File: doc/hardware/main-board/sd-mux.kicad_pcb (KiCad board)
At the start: 2 copper layers, 50 x 132 mm, 54 parts, among them J1 SDCARD, P1 USB_OTG, P10 MKDS 1,5/3, P2 629105136821, P3 61400416021, P4 61400416021, P5 IDC_02X04, P6 IDC_02X04, P7 MKDS 1,5/3, Q1 IRF7606PBF, Q2 IRF7606PBF, Q3 IRF7606PBF, Q4 IRF7606PBF, Q5 2N7002, Q6 2N7002, Q7 IRF7606PBF, Q8 IRF7606PBF, U1 TS3USB30EDGSR, U2 FT245RL, U3 74AHC1G14, U4 TS3A27518E, U5 74AHC1G14

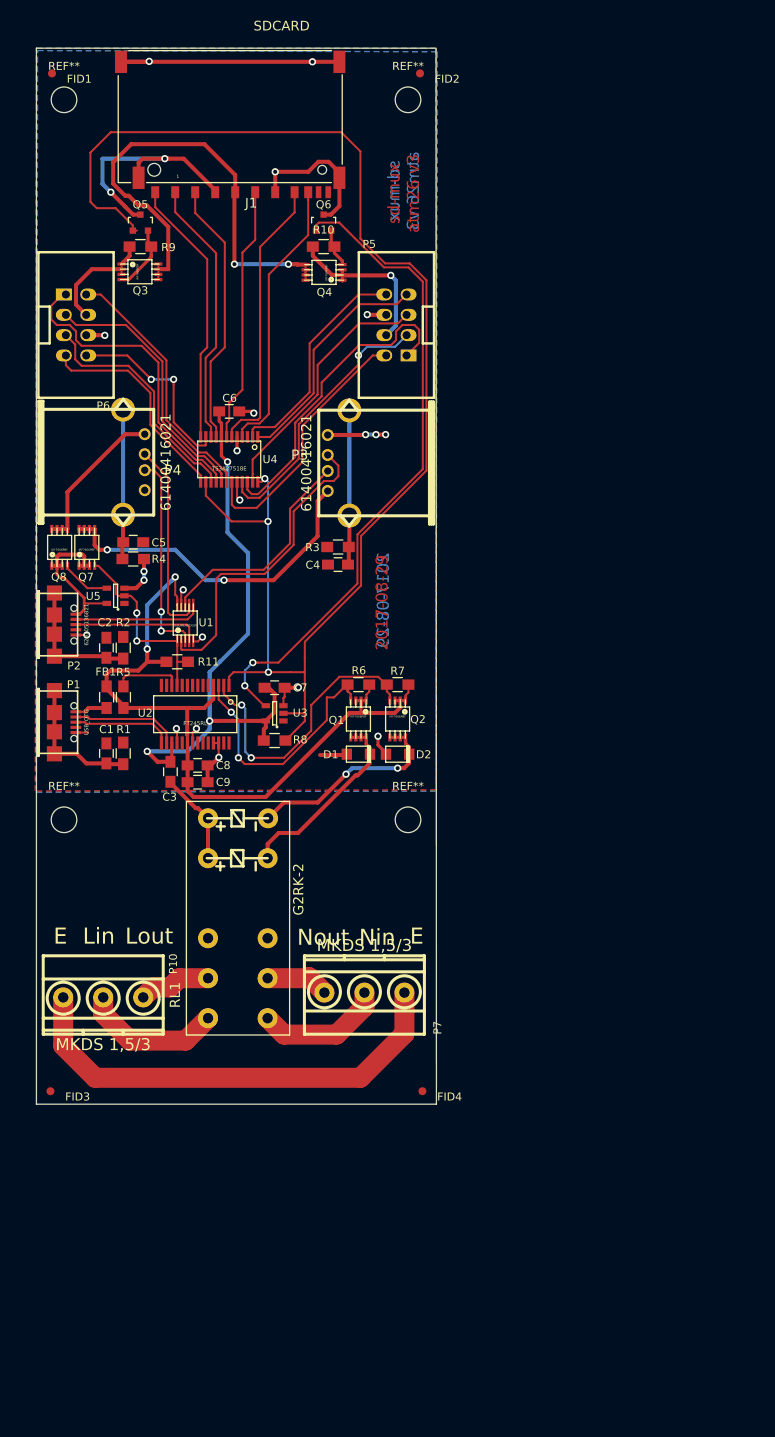
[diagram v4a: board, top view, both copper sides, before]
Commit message: Tweak pours to increase clearances.  Add some keepouts around ICs where lacking soldermask is likely to be problematic
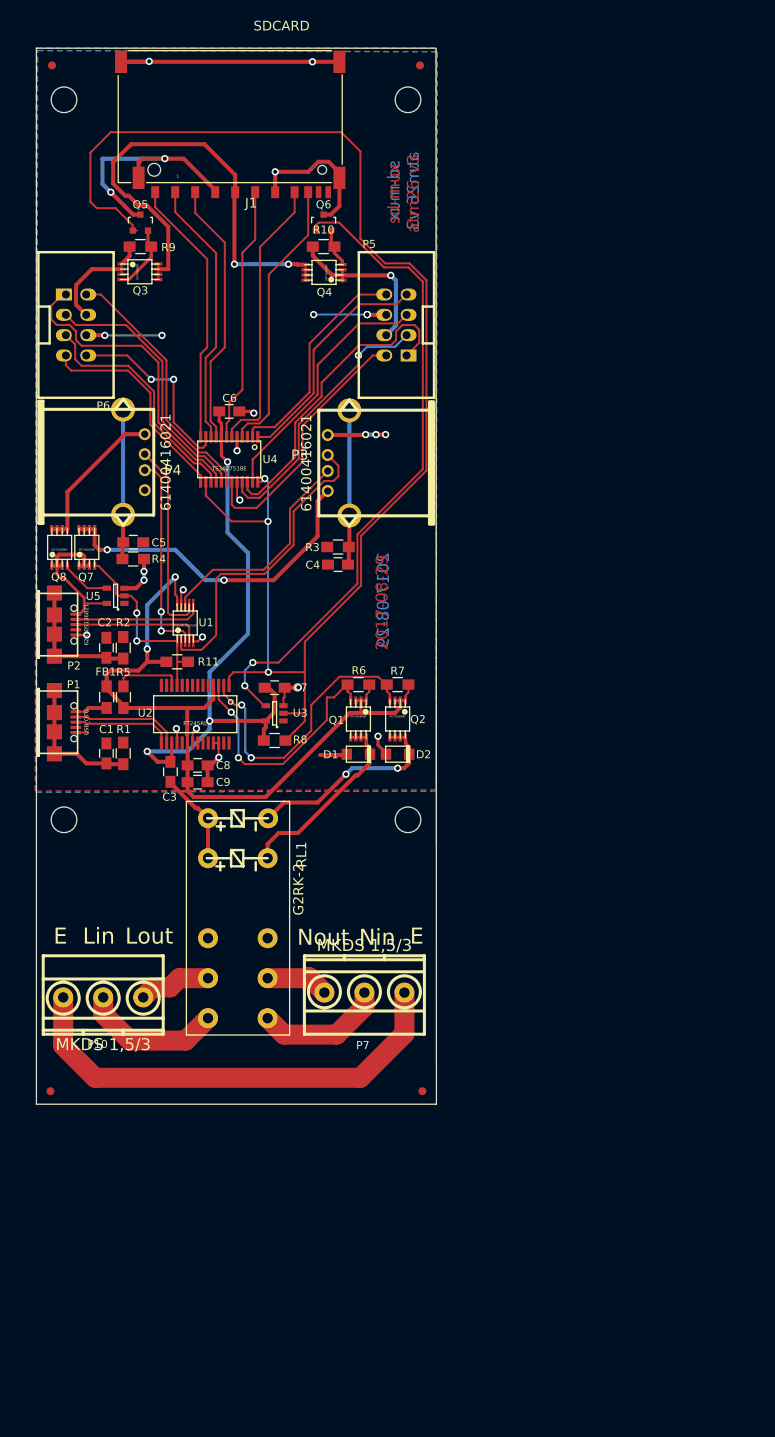
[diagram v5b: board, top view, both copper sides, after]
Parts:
- moved FID1 1.00 mm to (120.1, 17.8)
- moved FID2 1.00 mm to (166.1, 17.8)
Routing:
- net GND: track 143.3 -> 157.1 mm, vias 23 -> 26
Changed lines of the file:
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@@
     (thickness 1.6)
     (drawings 19)
-    (tracks 727)
+    (tracks 731)
     (zones 0)
     (modules 54)
@@
   )
   (setup
-    (last_trace_width 0.508)
+    (last_trace_width 0.254)
     (user_trace_width 0.508)
     (user_trace_width 1.116)
     (user_trace_width 2.5)
     (trace_clearance 0.2)
-    (zone_clearance 0.254)
+    (zone_clearance 0.508)
     (zone_45_only yes)
     (trace_min 0.254)
@@
     (pcbplotparams
       (layerselection 0x010fc_80000001)
-      (usegerberextensions false)
+      (usegerberextensions true)
       (excludeedgelayer false)
       (linewidth 0.100000)
@@
       (drillshape 0)
       (scaleselection 1)
-      (outputdirectory fabr/))
+      (outputdirectory ../fabrication/sd-mux-atm26-v3/))
   )
   (net 0 "")
@@
     (descr "Mounting Hole 3.2mm, no annular, M3")
     (tags "mounting hole 3.2mm no annular m3")
-    (fp_text reference REF** (at 0 -4.2) (layer F.SilkS)
+    (fp_text reference REF** (at 0 -4.2) (layer F.SilkS) hide
       (effects (font (size 1 1) (thickness 0.15)))
     )
@@
     (descr "Mounting Hole 3.2mm, no annular, M3")
     (tags "mounting hole 3.2mm no annular m3")
-    (fp_text reference REF** (at 0 -4.2) (layer F.SilkS)
+    (fp_text reference REF** (at 0 -4.2) (layer F.SilkS) hide
       (effects (font (size 1 1) (thickness 0.15)))
     )
@@
     (descr "Mounting Hole 3.2mm, no annular, M3")
     (tags "mounting hole 3.2mm no annular m3")
-    (fp_text reference REF** (at 0 -4.2) (layer F.SilkS)
+    (fp_text reference REF** (at 0 -4.2) (layer F.SilkS) hide
       (effects (font (size 1 1) (thickness 0.15)))
     )
@@
     (tags marker)
     (attr virtual)
-    (fp_text reference FID3 (at 3.4 0.7) (layer F.SilkS)
+    (fp_text reference FID3 (at 3.4 0.7) (layer F.SilkS) hide
       (effects (font (size 1 1) (thickness 0.15)))
     )
@@
     (at 159.19952 133.65048 180)
     (descr "3 Pins 5mm screw connector")
-    (fp_text reference P7 (at -9.15048 -4.4 270) (layer F.SilkS)
+    (fp_text reference P7 (at 0.2 -6.6 360) (layer F.SilkS)
       (effects (font (size 1 1) (thickness 0.25)))
     )
@@
     (at 126.54952 134.25048)
     (descr "3 Pins 5mm screw connector")
-    (fp_text reference P10 (at 8.75048 -4.2 90) (layer F.SilkS)
+    (fp_text reference P10 (at -0.7 5.85 180) (layer F.SilkS)
       (effects (font (size 1 1) (thickness 0.25)))
     )
@@
     (at 143.39952 124.35048 270)
     (descr "relay, V23042-B2 series")
-    (fp_text reference RL1 (at 9.6 7.84952 270) (layer F.SilkS)
+    (fp_text reference RL1 (at -7.95 -7.95 270) (layer F.SilkS)
       (effects (font (thickness 0.3048)))
     )
@@
   )
   (module Fiducials:Fiducial_1mm_Dia_2.54mm_Outer_CopperTop (layer F.Cu)
-    (at 120.14952 18.75048)
+    (at 120.14952 17.75048)
     (descr "Circular Fiducial, 1mm bare copper top; 2.54mm keepout")
     (tags marker)
     (attr virtual)
-    (fp_text reference FID1 (at 3.4 0.7) (layer F.SilkS)
+    (fp_text reference FID1 (at 3.4 0.7) (layer F.SilkS) hide
       (effects (font (size 1 1) (thickness 0.15)))
     )
@@
   )
   (module Fiducials:Fiducial_1mm_Dia_2.54mm_Outer_CopperTop (layer F.Cu)
-    (at 166.14952 18.75048)
+    (at 166.14952 17.75048)
     (descr "Circular Fiducial, 1mm bare copper top; 2.54mm keepout")
     (tags marker)
     (attr virtual)
-    (fp_text reference FID2 (at 3.4 0.7) (layer F.SilkS)
+    (fp_text reference FID2 (at 3.4 0.7) (layer F.SilkS) hide
       (effects (font (size 1 1) (thickness 0.15)))
     )
@@
     (tags marker)
     (attr virtual)
-    (fp_text reference FID4 (at 3.4 0.7) (layer F.SilkS)
+    (fp_text reference FID4 (at 3.4 0.7) (layer F.SilkS) hide
       (effects (font (size 1 1) (thickness 0.15)))
     )
@@
     (descr "Mounting Hole 3.2mm, no annular, M3")
     (tags "mounting hole 3.2mm no annular m3")
-    (fp_text reference REF** (at 0 -4.2) (layer F.SilkS)
+    (fp_text reference REF** (at 0 -4.2) (layer F.SilkS) hide
       (effects (font (size 1 1) (thickness 0.15)))
     )
@@
   (segment (start 120.45 98.65112) (end 120.45 101.04888) (width 0.508) (layer F.Cu) (net 1))
   (segment (start 120.45 101.04888) (end 120.45 103.7997) (width 0.508) (layer F.Cu) (net 1))
+  (via (at 133.9 51.5) (size 0.91) (drill 0.5) (layers F.Cu B.Cu) (net 2))
+  (segment (start 126.75 51.5) (end 133.9 51.5) (width 0.254) (layer B.Cu) (net 2))
+  (via (at 152.85 48.9) (size 0.91) (drill 0.5) (layers F.Cu B.Cu) (net 2))
+  (segment (start 159.55 48.9) (end 152.85 48.9) (width 0.254) (layer B.Cu) (net 2))
+  (via (at 159.55 48.9) (size 0.91) (drill 0.5) (layers F.Cu B.Cu) (net 2))
   (segment (start 126.45852 29.40948) (end 126.45852 32.55948) (width 0.508) (layer B.Cu) (net 2))
   (segment (start 126.45852 32.55948) (end 127.49952 33.60048) (width 0.508) (layer B.Cu) (net 2))
@@
   (segment (start 145.22608 68.80975) (end 145.22608 69.79908) (width 0.254) (layer F.Cu) (net 27))
   (segment (start 164.47 48.93) (end 164.13 48.93) (width 0.254) (layer F.Cu) (net 27))
+  (segment (start 135.349996 57) (end 135.349996 62.358178) (width 0.254) (layer F.Cu) (net 28))
+  (segment (start 135.349996 62.358178) (end 138.542296 65.55048) (width 0.254) (layer F.Cu) (net 28))
+  (segment (start 138.542296 65.55048) (end 139.01369 65.55048) (width 0.254) (layer F.Cu) (net 28))
+  (segment (start 139.01369 65.55048) (end 139.37392 65.19025) (width 0.254) (layer F.Cu) (net 28))
+  (segment (start 139.37392 65.19025) (end 139.37392 64.20092) (width 0.254) (layer F.Cu) (net 28))
   (segment (start 135.349996 57) (end 134.706528 57.000001) (width 0.254) (layer B.Cu) (net 28))
   (segment (start 132.095 56.545002) (end 132.549999 57.000001) (width 0.254) (layer F.Cu) (net 28))
@@
   (segment (start 134.706528 57.000001) (end 133.193466 57.000001) (width 0.254) (layer B.Cu) (net 28))
   (via (at 132.549999 57.000001) (size 0.91) (drill 0.5) (layers F.Cu B.Cu) (net 28))
-  (segment (start 135.349996 62.358178) (end 135.349996 57.643467) (width 0.254) (layer F.Cu) (net 28))
-  (segment (start 138.255069 65.263251) (end 135.349996 62.358178) (width 0.254) (layer F.Cu) (net 28))
-  (segment (start 139.300919 65.263251) (end 138.255069 65.263251) (width 0.254) (layer F.Cu) (net 28))
-  (segment (start 139.37392 64.20092) (end 139.37392 65.19025) (width 0.254) (layer F.Cu) (net 28))
-  (segment (start 139.37392 65.19025) (end 139.300919 65.263251) (width 0.254) (layer F.Cu) (net 28))
-  (segment (start 135.349996 57.643467) (end 135.349996 57) (width 0.254) (layer F.Cu) (net 28))
   (via (at 135.349996 57) (size 0.91) (drill 0.5) (layers F.Cu B.Cu) (net 28))
   (segment (start 124.42952 54.00048) (end 124.42 54.01) (width 0.254) (layer B.Cu) (net 28))
@@
   (segment (start 126.54952 134.25048) (end 126.54952 136.30048) (width 2.5) (layer F.Cu) (net 74))
   (zone (net 2) (net_name GND) (layer F.Cu) (hatch edge 0.508)
-    (connect_pads (clearance 0.254))
-    (min_thickness 0.254)
-    (fill yes (arc_segments 16) (thermal_gap 0.3) (thermal_bridge_width 0.3) (smoothing fillet))
+    (connect_pads (clearance 0.5))
+    (min_thickness 0.5)
+    (fill yes (arc_segments 16) (thermal_gap 0.5) (thermal_bridge_width 0.55) (smoothing fillet))
     (polygon
       (pts
@@
   (zone (net 2) (net_name GND) (layer B.Cu) (hatch edge 0.508)
     (connect_pads (clearance 0.508))
-    (min_thickness 0.254)
-    (fill yes (arc_segments 16) (thermal_gap 0.3) (thermal_bridge_width 0.3) (smoothing fillet))
+    (min_thickness 0.5)
+    (fill yes (arc_segments 16) (thermal_gap 0.5) (thermal_bridge_width 0.55) (smoothing fillet))
     (polygon
       (pts
@@
       )
     )
+  )
+  (zone (net 0) (net_name "") (layer F.Cu) (hatch edge 0.508)
+    (connect_pads (clearance 0.254))
+    (min_thickness 0.254)
+    (keepout (tracks allowed) (vias allowed) (copperpour not_allowed))
+    (fill yes (arc_segments 16) (thermal_gap 0.508) (thermal_bridge_width 0.508))
+    (polygon
+      (pts
+        (xy 129.59952 41.70048) (xy 134.39952 41.70048) (xy 134.39952 45.30048) (xy 128.84952 45.30048) (xy 128.69952 41.70048)
+      )
+    )
+  )
+  (zone (net 0) (net_name "") (layer F.Cu) (hatch edge 0.508)
+    (connect_pads (clearance 0.254))
+    (min_thickness 0.254)
+    (keepout (tracks allowed) (vias allowed) (copperpour not_allowed))
+    (fill yes (arc_segments 16) (thermal_gap 0.508) (thermal_bridge_width 0.508))
+    (polygon
+      (pts
+        (xy 150.59952 41.70048) (xy 157.34952 41.70048) (xy 157.34952 45.30048) (xy 150.59952 45.30048)
+      )
+    )
+  )
+  (zone (net 0) (net_name "") (layer F.Cu) (hatch edge 0.508)
+    (connect_pads (clearance 0.254))
+    (min_thickness 0.254)
+    (keepout (tracks allowed) (vias allowed) (copperpour not_allowed))
+    (fill yes (arc_segments 16) (thermal_gap 0.508) (thermal_bridge_width 0.508))
+    (polygon
+      (pts
+        (xy 138.14952 63.00048) (xy 146.39952 63.00048) (xy 146.39952 65.40048) (xy 137.99952 65.40048) (xy 137.99952 63.00048)
+      )
+    )
+  )
+  (zone (net 0) (net_name "") (layer F.Cu) (hatch edge 0.508)
+    (connect_pads (clearance 0.254))
+    (min_thickness 0.254)
+    (keepout (tracks allowed) (vias allowed) (copperpour not_allowed))
+    (fill yes (arc_segments 16) (thermal_gap 0.508) (thermal_bridge_width 0.508))
+    (polygon
+      (pts
+        (xy 137.99952 68.55048) (xy 146.69952 68.55048) (xy 146.69952 71.10048) (xy 137.99952 70.95048)
+      )
+    )
